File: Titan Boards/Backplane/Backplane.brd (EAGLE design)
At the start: 195.1 x 76.2 mm, 29 parts, among them P1 39-30-02?_S, P3 39-30-04?_S

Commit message: First final version of Titan Backplane Schematic
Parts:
- added ACT_CONN_LED, BB_CONN_LED, COPRO_CONN_LED, ESC_CONN_LED: (no value), led:CHIP-LED0603
- added R19, R20, R21, R22: 36, rcl:R0603
- renumbered P1 to 5V_CONNECTOR, P3 to 3.3V_CONNECTOR, U$5 to KILLSWITCH_CONNECTOR, U$6 to THRUSTER_CONNECTOR, U$7 to ENABLE_SIGNALS_CONNECTOR, U$8 to I2C_CONNECTOR
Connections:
- removed net SPARE7: KILLSWITCH_CONNECTOR.P$1, U$1.43, U$2.43, U$3.43, U$4.43
- new net ACT_CONN: ACT_CONN_LED.A, U$4.43
- new net BB_CONN: BB_CONN_LED.A, U$1.43
- new net COPRO_CONN: COPRO_CONN_LED.A, U$3.43
- new net ESC_CONN: ESC_CONN_LED.A, U$2.43
- new net N$12: BB_CONN_LED.C, R19.1
- new net N$13: ESC_CONN_LED.C, R20.1
- new net N$14: COPRO_CONN_LED.C, R21.1
- new net N$15: ACT_CONN_LED.C, R22.1
- net GND: now also R19.2, R20.2, R21.2, R22.2

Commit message: Titan Backplane Final Version 1
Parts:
- removed 3.3V_CONNECTOR: 39-30-04?_S, con-molex-mini-fit:39-30-?04?
- removed ENABLE_SIGNALS_CONNECTOR: 929870-01-09_3, 3M_929852_Connector:929852-01-09_1ROW
- removed I2C_CONNECTOR: 929870-01-09_4, 3M_929852_Connector:929852-01-09_1ROW
- removed KILLSWITCH_CONNECTOR: 929870-01-09_1, 3M_929852_Connector:929852-01-09_1ROW
- removed R1, R10, R11, R12, R13, R14, R2, R3, R4, R5, R6, R7, R8, R9: 10k, rcl:R0603
- removed THRUSTER_CONNECTOR: 929870-01-09_2, 3M_929852_Connector:929852-01-09_1ROW
- added AUX_I2C_CONNECTOR1, ROBOT_I2C_CONNECTOR: 39-30-04?_S, con-molex-mini-fit:39-30-?04?
- added TESTPIN_CONNECTOR: 929870-01-09_4, 3M_929852_Connector:929852-01-09_1ROW
- SWITCH_CONNECTOR: value 39-30-08?_S -> 39-30-02?_S; device con-molex-mini-fit:39-30-?08? -> con-molex-mini-fit:39-30-?02?
- moved COPRO_CONN_LED 763.8 mm to (88.5, 58.7)
- moved R21 751.4 mm to (90.4, 58.3), turned to 270 degrees
- moved R19 736.0 mm to (119.1, 58.5), turned to 270 degrees
- moved BB_CONN_LED 732.3 mm to (121.0, 58.4)
- moved R22 727.9 mm to (90.3, 18.4), turned to 270 degrees
- moved ACT_CONN_LED 723.2 mm to (88.5, 18.2)
- moved ESC_CONN_LED 712.5 mm to (121.0, 17.8)
- moved R20 700.3 mm to (119.3, 17.8), turned to 270 degrees
- moved U$3 643.8 mm to (16.5, 55.9)
- moved U$1 631.0 mm to (124.5, 55.9)
- moved R17 616.9 mm to (54.7, 4.45), turned to 270 degrees
- moved R18 616.7 mm to (57.3, 4.45), turned to 270 degrees
- moved U$4 615.3 mm to (16.5, 15.2)
- moved R15 611.4 mm to (49.7, 4.45), turned to 270 degrees
- moved R16 611.2 mm to (52.2, 4.45), turned to 270 degrees
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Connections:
- net 12V_ON/OFF: no longer ENABLE_SIGNALS_CONNECTOR.P$3
- net 3.3V: now also AUX_I2C_CONNECTOR1.1, ROBOT_I2C_CONNECTOR.1, TESTPIN_CONNECTOR.P$7; no longer 3.3V_CONNECTOR.1, I2C_CONNECTOR.P$7, R10.1, R11.1, R12.1, R13.1, R14.1, R9.1
- net 3.3V_ON/OFF: no longer ENABLE_SIGNALS_CONNECTOR.P$1
- net 5V: now also SWITCH_CONNECTOR.1, TESTPIN_CONNECTOR.P$9; no longer I2C_CONNECTOR.P$9, R1.1, R2.1, R3.1, R4.1, R5.1, R6.1, R7.1, R8.1
- net 5V_ON/OFF: no longer ENABLE_SIGNALS_CONNECTOR.P$2
- net ACOUSTIC_ON/OFF: no longer ENABLE_SIGNALS_CONNECTOR.P$4
- net BACKPLANE_SCL: now also TESTPIN_CONNECTOR.P$4; no longer I2C_CONNECTOR.P$4
- net BACKPLANE_SDA: now also TESTPIN_CONNECTOR.P$3; no longer I2C_CONNECTOR.P$3
- net CONTROL_SIGNAL: no longer ENABLE_SIGNALS_CONNECTOR.P$7
- net GND: now also AUX_I2C_CONNECTOR1.3, ROBOT_I2C_CONNECTOR.3, SWITCH_CONNECTOR.2, TESTPIN_CONNECTOR.P$8; no longer 3.3V_CONNECTOR.3, ENABLE_SIGNALS_CONNECTOR.P$9, I2C_CONNECTOR.P$8, SWITCH_CONNECTOR.5
- net JETSON_ON/OFF: no longer ENABLE_SIGNALS_CONNECTOR.P$5
- net KILL_SWITCH: no longer KILLSWITCH_CONNECTOR.P$7, R9.2, SWITCH_CONNECTOR.2
- net MOBO_ON/OFF: no longer ENABLE_SIGNALS_CONNECTOR.P$6
- net PLTA_ON/OFF: no longer ENABLE_SIGNALS_CONNECTOR.P$8, SWITCH_CONNECTOR.1
- net PWM_1: no longer R1.2, THRUSTER_CONNECTOR.P$9
- net PWM_2: no longer R2.2, THRUSTER_CONNECTOR.P$8
- net PWM_3: no longer R3.2, THRUSTER_CONNECTOR.P$7
- net PWM_4: no longer R4.2, THRUSTER_CONNECTOR.P$6
- net PWM_5: no longer R5.2, THRUSTER_CONNECTOR.P$5
- net PWM_6: no longer R6.2, THRUSTER_CONNECTOR.P$4
- net PWM_7: no longer R7.2, THRUSTER_CONNECTOR.P$3
- net PWM_8: no longer R8.2, THRUSTER_CONNECTOR.P$2
- net ROBOT_SCL: now also AUX_I2C_CONNECTOR1.4, ROBOT_I2C_CONNECTOR.4, TESTPIN_CONNECTOR.P$6; no longer 3.3V_CONNECTOR.4, I2C_CONNECTOR.P$6
- net ROBOT_SDA: now also AUX_I2C_CONNECTOR1.2, ROBOT_I2C_CONNECTOR.2, TESTPIN_CONNECTOR.P$5; no longer 3.3V_CONNECTOR.2, I2C_CONNECTOR.P$5
- net SPARE2: no longer THRUSTER_CONNECTOR.P$1
- net SPARE3: now also TESTPIN_CONNECTOR.P$2; no longer I2C_CONNECTOR.P$2
- net SPARE4: now also TESTPIN_CONNECTOR.P$1; no longer I2C_CONNECTOR.P$1
- net SPARE5: no longer KILLSWITCH_CONNECTOR.P$9
- net SPARE6: no longer KILLSWITCH_CONNECTOR.P$8
- net SWITCH_1: no longer KILLSWITCH_CONNECTOR.P$6, R10.2, SWITCH_CONNECTOR.3
- net SWITCH_2: no longer KILLSWITCH_CONNECTOR.P$5, R11.2, SWITCH_CONNECTOR.4
- net SWITCH_3: no longer KILLSWITCH_CONNECTOR.P$4, R12.2, SWITCH_CONNECTOR.6
- net SWITCH_4: no longer KILLSWITCH_CONNECTOR.P$3, R13.2, SWITCH_CONNECTOR.7
- net SWITCH_5: no longer KILLSWITCH_CONNECTOR.P$2, R14.2, SWITCH_CONNECTOR.8
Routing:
- net GND: track 0.00 -> 479.0 mm, vias 0 -> 8
- net 3.3V: track 0.00 -> 335.0 mm, vias 0 -> 2
- net ROBOT_SDA: track 0.00 -> 316.8 mm, vias 0 -> 5
- net 5V: track 0.00 -> 316.1 mm, vias 0 -> 3
- net ROBOT_SCL: track 0.00 -> 311.8 mm, vias 0 -> 2
- net BACKPLANE_SDA: track 0.00 -> 296.1 mm, vias 0 -> 5
- net BACKPLANE_SCL: track 0.00 -> 295.3 mm, vias 0 -> 5
- net SPARE4: track 0.00 -> 279.8 mm, vias 0 -> 4
- net SPARE3: track 0.00 -> 279.0 mm, vias 0 -> 4
- net PLTA_ON/OFF: track 0.00 -> 273.3 mm, vias 0 -> 4
- net CONTROL_SIGNAL: track 0.00 -> 272.1 mm, vias 0 -> 4
- net 3.3V_ON/OFF: track 0.00 -> 271.1 mm, vias 0 -> 4
- net SWITCH_5: track 0.00 -> 270.2 mm, vias 0 -> 4
- net 5V_ON/OFF: track 0.00 -> 270.2 mm, vias 0 -> 4
- net SWITCH_4: track 0.00 -> 269.2 mm, vias 0 -> 4
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- added copper zone on layer 1, net 3.3V
- added copper zone on layer 1, net 5V
- added copper zone on layer 1, net GND
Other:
- board size 195.1 x 76.2 mm -> 209.6 x 76.2 mm
- board text added: "3.3V"
- board text added: "5V"
- board text added: "BPlane SCL"
- board text added: "BPlane SDA"
- board text added: "Backplane"
- board text added: "GND"
- board text added: "Robot SCL"
- board text added: "Robot SDA"
- board text added: "Spare 3"
- board text added: "Spare 4"
- board text removed: "Board Name HERE!!!"

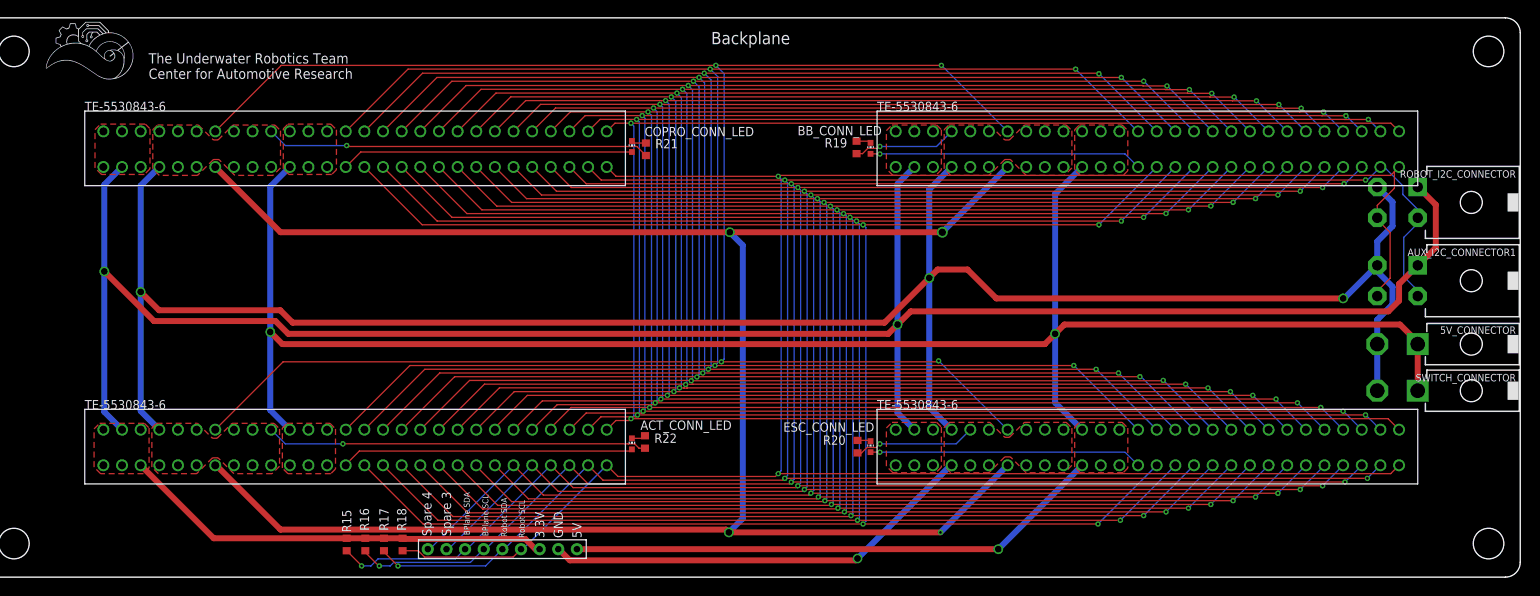
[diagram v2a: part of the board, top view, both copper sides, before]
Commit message: Backplane connector and spacing revisions
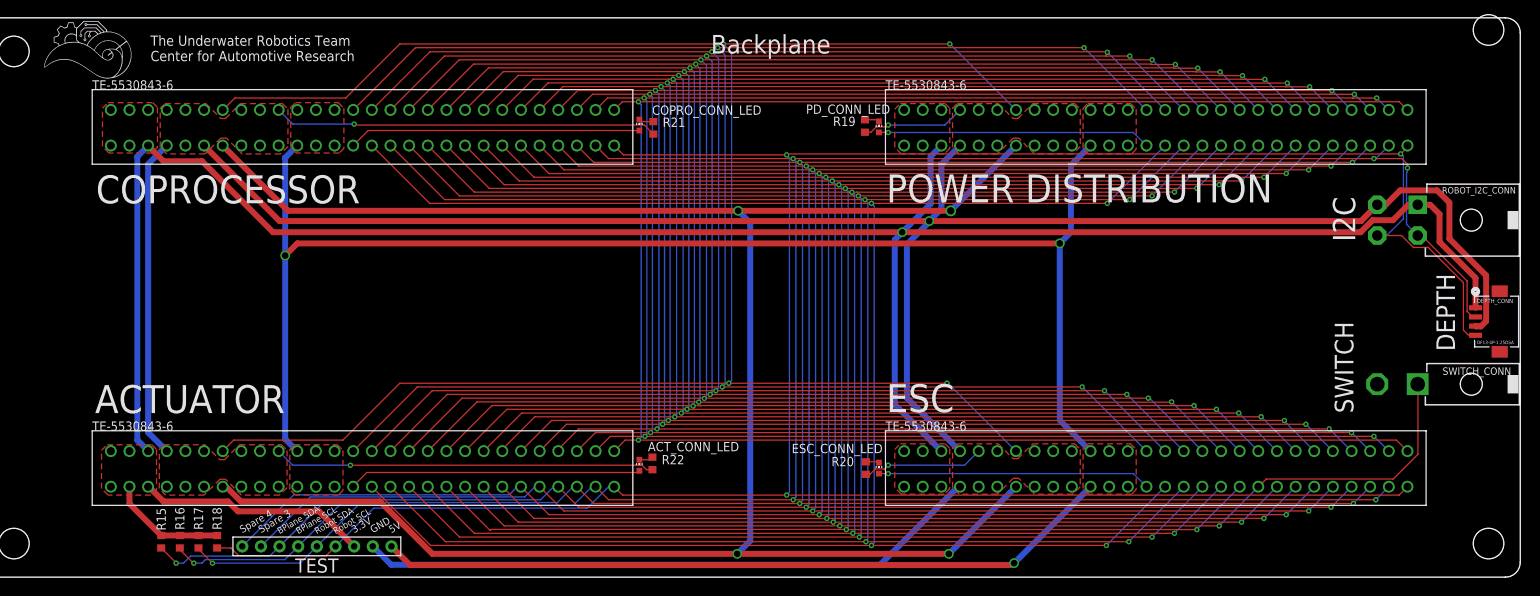
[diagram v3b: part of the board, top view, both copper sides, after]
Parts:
- removed 5V_CONNECTOR, SWITCH_CONNECTOR: 39-30-02?_S, con-molex-mini-fit:39-30-?02?
- removed AUX_I2C_CONNECTOR1, ROBOT_I2C_CONNECTOR: 39-30-04?_S, con-molex-mini-fit:39-30-?04?
- removed BB_CONN_LED: (no value), led:CHIP-LED0603
- added DEPTH_CONN: DF13-4P-1.25DSA, DF13-4P-125DSA_Connector:CON4_1X4_U_DF13
- added PD_CONN_LED: (no value), led:CHIP-LED0603
- added ROBOT_I2C_CONN: 39-30-04?_S, con-molex-mini-fit:39-30-?04?
- added SWITCH_CONN: 39-30-02?_S, con-molex-mini-fit:39-30-?02?
- moved R16 25.3 mm to (26.9, 4.83)
- moved R17 25.3 mm to (29.5, 4.83)
- moved R18 25.3 mm to (32.0, 4.83)
- moved TESTPIN_CONNECTOR 25.3 mm to (34.2, 2.92)
- moved R15 25.3 mm to (24.4, 4.83)
- moved R19 3.14 mm to (120.3, 61.5)
- moved ESC_CONN_LED 3.14 mm to (122.2, 14.9)
- moved R20 3.14 mm to (120.4, 14.9)
- moved U$1 3.14 mm to (125.6, 58.8)
- moved U$2 3.14 mm to (125.6, 12.3)
- moved R22 3.09 mm to (91.3, 15.5)
- moved U$3 3.09 mm to (17.5, 58.8)
- moved U$4 3.09 mm to (17.5, 12.3)
- moved ACT_CONN_LED 3.09 mm to (89.5, 15.2)
- moved COPRO_CONN_LED 3.09 mm to (89.5, 61.6)
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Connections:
- new net EXTRA_AUXILLARY: SWITCH_CONN.2
- net 3.3V: now also DEPTH_CONN.1, ROBOT_I2C_CONN.1; no longer AUX_I2C_CONNECTOR1.1, ROBOT_I2C_CONNECTOR.1
- net 5V: no longer 5V_CONNECTOR.1, SWITCH_CONNECTOR.1
- net BB_CONN: now also PD_CONN_LED.A; no longer BB_CONN_LED.A
- net GND: now also DEPTH_CONN.3, ROBOT_I2C_CONN.3; no longer 5V_CONNECTOR.2, AUX_I2C_CONNECTOR1.3, ROBOT_I2C_CONNECTOR.3, SWITCH_CONNECTOR.2
- net KILL_SWITCH: now also SWITCH_CONN.1
- net N$12: now also PD_CONN_LED.C; no longer BB_CONN_LED.C
- net ROBOT_SCL: now also DEPTH_CONN.4, ROBOT_I2C_CONN.4; no longer AUX_I2C_CONNECTOR1.4, ROBOT_I2C_CONNECTOR.4
- net ROBOT_SDA: now also DEPTH_CONN.2, ROBOT_I2C_CONN.2; no longer AUX_I2C_CONNECTOR1.2, ROBOT_I2C_CONNECTOR.2
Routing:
- net ROBOT_SCL: track 311.8 -> 360.4 mm, vias 2 -> 3
- net KILL_SWITCH: track 265.7 -> 304.9 mm
- net ROBOT_SDA: track 316.8 -> 355.4 mm, vias 5 -> 6
- net SPARE4: track 279.8 -> 310.6 mm
- net BACKPLANE_SDA: track 296.1 -> 326.9 mm
- net SPARE3: track 279.0 -> 309.8 mm
- net BACKPLANE_SCL: track 295.3 -> 326.1 mm
- net GND: track 479.0 -> 508.4 mm, vias 8 -> 5
- net 5V: track 316.1 -> 295.0 mm
- net SWITCH_1: track 266.6 -> 272.7 mm
- net JETSON_ON/OFF: track 267.2 -> 273.3 mm
- net 12V_ON/OFF: track 269.1 -> 275.2 mm
- net SWITCH_5: track 270.2 -> 276.3 mm
- net SWITCH_4: track 269.2 -> 275.3 mm
- net SPARE2: track 258.6 -> 264.7 mm
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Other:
- board text added: "ACTUATOR"
- board text added: "COPROCESSOR"
- board text added: "DEPTH"
- board text added: "ESC"
- board text added: "I2C"
- board text added: "POWER DISTRIBUTION"
- board text added: "SWITCH"
- board text added: "TEST"

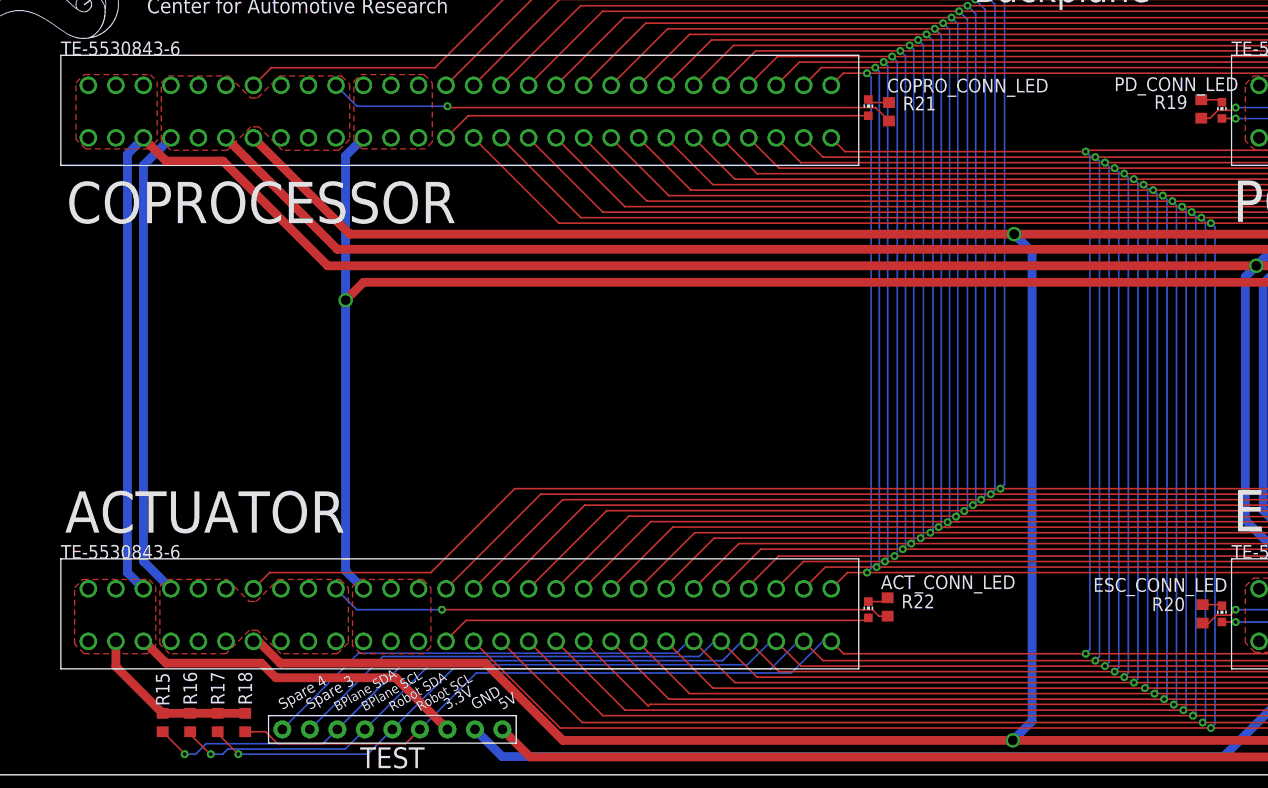
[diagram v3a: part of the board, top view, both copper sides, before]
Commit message: switched actuator and copro backplane connectors
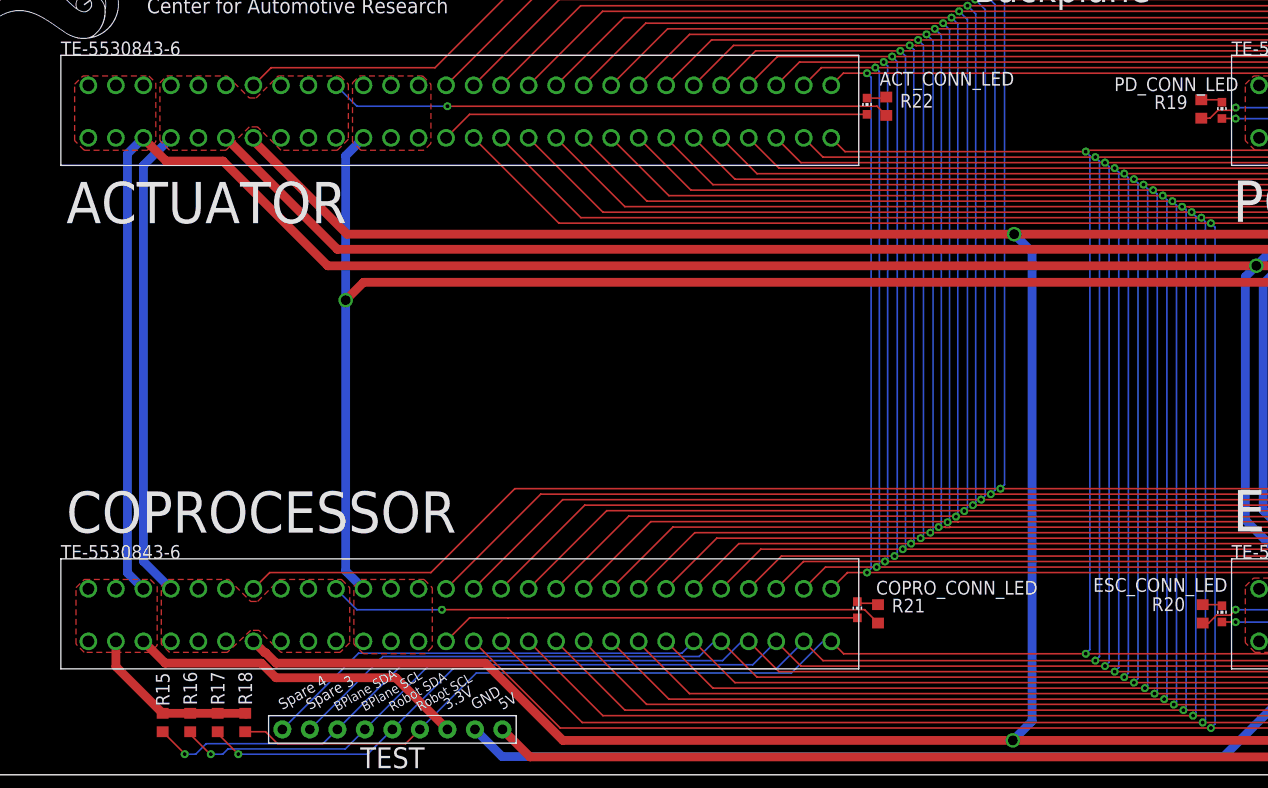
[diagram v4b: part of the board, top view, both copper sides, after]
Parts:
- moved ACT_CONN_LED 46.5 mm to (89.4, 61.7)
- moved U$3 46.5 mm to (17.5, 12.3)
- moved U$4 46.5 mm to (17.5, 58.8)
- moved COPRO_CONN_LED 46.4 mm to (88.5, 15.2)
- moved R21 46.4 mm to (90.4, 14.9)
- moved R22 46.2 mm to (91.2, 61.7)
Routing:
- net GND: track 508.4 -> 507.3 mm
- net COPRO_CONN: track 39.8 -> 38.9 mm
- net ROBOT_SCL: track 360.4 -> 359.6 mm
- net SPARE3: track 309.8 -> 309.1 mm
- net BACKPLANE_SDA: track 326.9 -> 326.2 mm

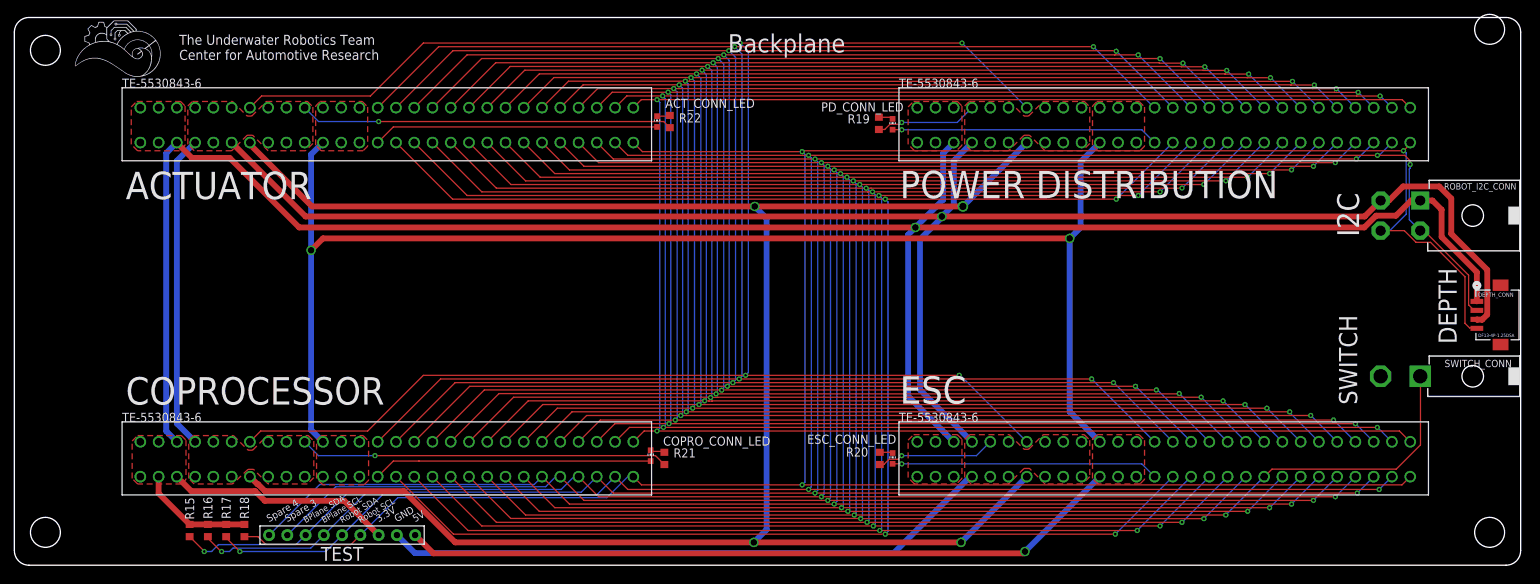
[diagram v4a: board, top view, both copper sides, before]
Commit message: backplane reorientation changes
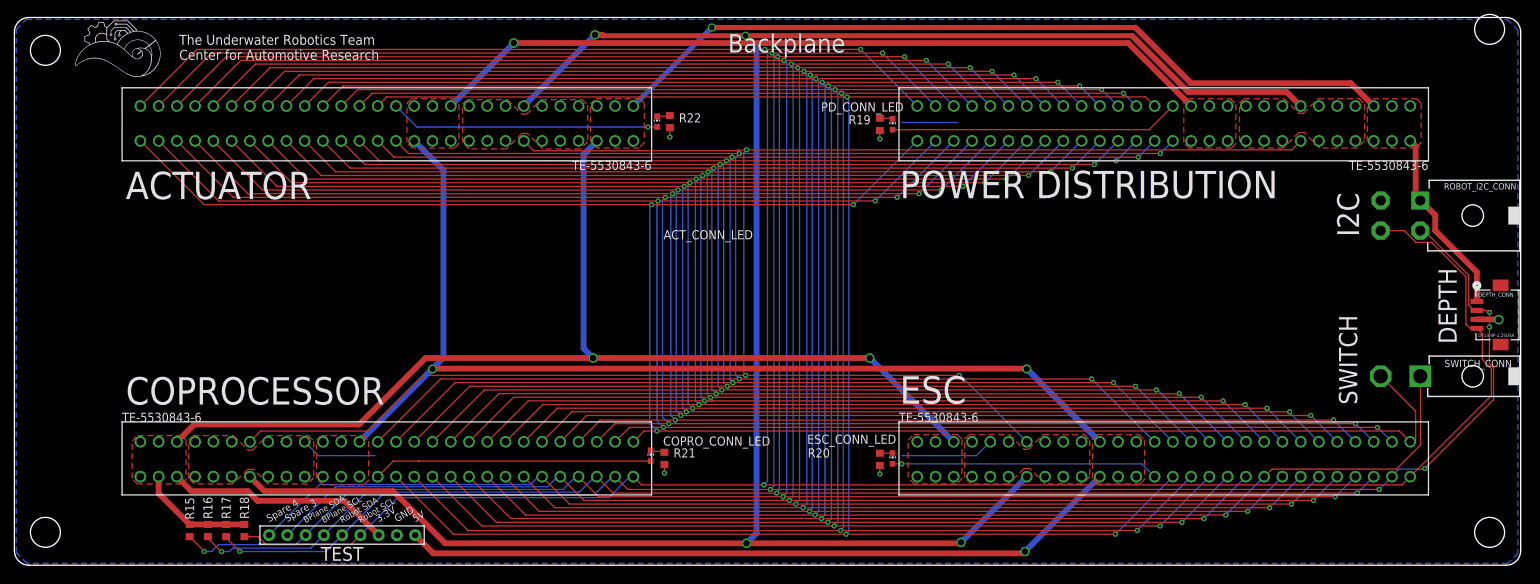
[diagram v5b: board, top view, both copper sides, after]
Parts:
- moved U$1 68.8 mm to (194.2, 63.9), turned to 180 degrees
- moved U$4 68.8 mm to (86.1, 63.9), turned to 180 degrees
- moved R19 0.18 mm to (120.4, 61.3)
- moved R20 0.13 mm to (120.4, 14.7)
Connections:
- removed net EXTRA_AUXILLARY: SWITCH_CONN.2
- net SPARE2: now also SWITCH_CONN.2
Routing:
- net GND: track 507.3 -> 39.3 mm
- net 5V: track 295.0 -> 356.5 mm, vias 3 -> 4
- net ROBOT_SDA: track 355.4 -> 391.9 mm, vias 6 -> 8
- net ROBOT_SCL: track 359.6 -> 393.9 mm
- net PLTA_ON/OFF: track 278.8 -> 303.9 mm
- net CONTROL_SIGNAL: track 278.1 -> 256.6 mm, vias 4 -> 3
- net 3.3V_ON/OFF: track 277.2 -> 256.6 mm
- net 5V_ON/OFF: track 276.3 -> 256.5 mm
- net 12V_ON/OFF: track 275.2 -> 256.6 mm
- net BACKPLANE_SCL: track 326.1 -> 344.1 mm
- net BACKPLANE_SDA: track 326.2 -> 344.1 mm
- net ACOUSTIC_ON/OFF: track 274.4 -> 256.5 mm
- net SPARE3: track 309.1 -> 326.1 mm
- net JETSON_ON/OFF: track 273.3 -> 256.6 mm
- net MOBO_ON/OFF: track 272.5 -> 256.5 mm
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- added copper zone on layer 16, net GND

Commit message: final backplane fixes
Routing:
- net GND: track 39.3 -> 7.92 mm
- net ROBOT_SCL: track 393.9 -> 392.1 mm
